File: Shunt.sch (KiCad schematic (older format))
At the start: 1 part

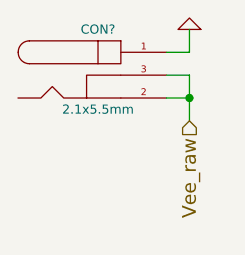
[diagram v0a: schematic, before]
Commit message: breaking out additional subsheets.  specifying transistor values.
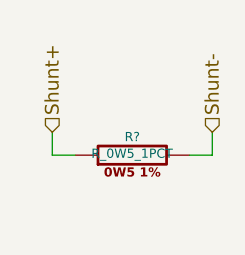
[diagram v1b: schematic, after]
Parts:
- removed CON?: 2.1x5.5mm, ~, symbol BARREL_JACK
- added R?: R_0W5_1PCT, ~, symbol R_0W5_1PCT
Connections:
- new net Shunt+: R?.1
- new net Shunt-: R?.2
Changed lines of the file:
@@
 $Descr A4 11693 8268
 encoding utf-8
-Sheet 5 9
+Sheet 8 9
 Title ""
 Date "29 mar 2014"
@@
 $EndDescr
 $Comp
-L BARREL_JACK CON?
-U 1 1 5337866E
-P 5450 3550
-F 0 "CON?" H 5450 3750 40  0000 C CNN
-F 1 "2.1x5.5mm" H 5450 3400 40  0000 C CNN
-F 2 "~" H 5450 3550 60  0000 C CNN
-F 3 "~" H 5450 3550 60  0000 C CNN
-	1    5450 3550
-	1    0    0    -1
-$EndComp
-$Comp
-L GND #PWR?
-U 1 1 53378674
-P 5850 3350
-F 0 "#PWR?" H 5850 3350 30  0001 C CNN
-F 1 "GND" H 5850 3280 30  0001 C CNN
-F 2 "" H 5850 3350 60  0000 C CNN
-F 3 "" H 5850 3350 60  0000 C CNN
-	1    5850 3350
-	-1   0    0    1
+L R_0W5_1PCT R?
+U 1 1 53383531
+P 5600 3900
+F 0 "R?" V 5680 3900 40  0000 C CNN
+F 1 "R_0W5_1PCT" V 5607 3901 40  0000 C CNN
+F 2 "~" V 5530 3900 30  0000 C CNN
+F 3 "~" H 5600 3900 30  0000 C CNN
+	1    5600 3900
+	0    -1   -1   0
 $EndComp
 Wire Wire Line
-	5750 3450 5850 3450
+	5250 3800 5250 3900
 Wire Wire Line
-	5850 3450 5850 3350
+	5950 3800 5950 3900
 Wire Wire Line
-	5750 3650 5850 3650
+	5250 3900 5350 3900
 Wire Wire Line
-	5850 3550 5850 3750
-Wire Wire Line
-	5750 3550 5850 3550
-Connection ~ 5850 3650
-Text HLabel 5850 3750 3    60   Input ~ 0
-Vee_raw
+	5950 3900 5850 3900
+Text HLabel 5250 3800 1    60   Input ~ 0
+Shunt+
+Text HLabel 5950 3800 1    60   Input ~ 0
+Shunt-
 $EndSCHEMATC

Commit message: working on revamp of power supply.
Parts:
- removed R?: R_0W5_1PCT, ~, symbol R_0W5_1PCT
- added R? (x10): 1, ~, symbol R_0W25_1PCT
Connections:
- net Shunt+: now also R?.1, R?.1, R?.1, R?.1, R?.1, R?.1, R?.1, R?.1, R?.1, R?.1
- net Shunt-: now also R?.2, R?.2, R?.2, R?.2, R?.2, R?.2, R?.2, R?.2, R?.2, R?.2
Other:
- note added: "0.1 Ohm, 2.5 Watt shunt\n(5A max)"
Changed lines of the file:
@@
 EESchema Schematic File Version 2
+LIBS:references_PL
+LIBS:OpAmpPassXsistorBenchSupply-cache
 LIBS:opamps_PL
+LIBS:opto_PL
+LIBS:regulators_PL
+LIBS:relays_PL
+LIBS:resistors_PL
+LIBS:switches_PL
 LIBS:transistors_PL
+LIBS:analog_ICs_PL
+LIBS:capacitors_PL
+LIBS:connectors_PL
 LIBS:diodes_PL
-LIBS:resistors_PL
-LIBS:capacitors_PL
-LIBS:regulators_PL
-LIBS:connectors_PL
+LIBS:displays_PL
+LIBS:LEDs_PL
+LIBS:microcontrollers_PL
+LIBS:mounting_holes_PL
 LIBS:power
 LIBS:device
@@
 $Descr A4 11693 8268
 encoding utf-8
-Sheet 8 9
+Sheet 4 2
 Title ""
 Date "4 jul 2014"
@@
 Comment4 ""
 $EndDescr
-$Comp
-L R_0W5_1PCT R?
-U 1 1 53383531
+Wire Wire Line
+	5150 3800 5150 3900
+Wire Wire Line
+	6050 3800 6050 3900
+Wire Wire Line
+	5150 3900 5350 3900
+Wire Wire Line
+	6050 3900 5850 3900
+Text HLabel 5150 3800 1    60   Input ~ 0
+Shunt+
+Text HLabel 6050 3800 1    60   Input ~ 0
+Shunt-
+$Comp
+L R_0W25_1PCT R?
+U 1 1 53B6360E
 P 5600 3900
 F 0 "R?" V 5680 3900 40  0000 C CNN
-F 1 "R_0W5_1PCT" V 5607 3901 40  0000 C CNN
+F 1 "1" V 5607 3901 40  0000 C CNN
 F 2 "~" V 5530 3900 30  0000 C CNN
 F 3 "~" H 5600 3900 30  0000 C CNN
@@
 	0    -1   -1   0
 $EndComp
-Wire Wire Line
-	5250 3800 5250 3900
-Wire Wire Line
-	5950 3800 5950 3900
-Wire Wire Line
-	5250 3900 5350 3900
-Wire Wire Line
-	5950 3900 5850 3900
-Text HLabel 5250 3800 1    60   Input ~ 0
-Shunt+
-Text HLabel 5950 3800 1    60   Input ~ 0
-Shunt-
+$Comp
+L R_0W25_1PCT R?
+U 1 1 53B63620
+P 5600 4150
+F 0 "R?" V 5680 4150 40  0000 C CNN
+F 1 "1" V 5607 4151 40  0000 C CNN
+F 2 "~" V 5530 4150 30  0000 C CNN
+F 3 "~" H 5600 4150 30  0000 C CNN
+	1    5600 4150
+	0    -1   -1   0
+$EndComp
+$Comp
+L R_0W25_1PCT R?
+U 1 1 53B63626
+P 5600 4400
+F 0 "R?" V 5680 4400 40  0000 C CNN
+F 1 "1" V 5607 4401 40  0000 C CNN
+F 2 "~" V 5530 4400 30  0000 C CNN
+F 3 "~" H 5600 4400 30  0000 C CNN
+	1    5600 4400
+	0    -1   -1   0
+$EndComp
+$Comp
+L R_0W25_1PCT R?
+U 1 1 53B6362C
+P 5600 3650
+F 0 "R?" V 5680 3650 40  0000 C CNN
+F 1 "1" V 5607 3651 40  0000 C CNN
+F 2 "~" V 5530 3650 30  0000 C CNN
+F 3 "~" H 5600 3650 30  0000 C CNN
+	1    5600 3650
+	0    -1   -1   0
+$EndComp
+$Comp
+L R_0W25_1PCT R?
+U 1 1 53B63632
+P 5600 3400
+F 0 "R?" V 5680 3400 40  0000 C CNN
+F 1 "1" V 5607 3401 40  0000 C CNN
+F 2 "~" V 5530 3400 30  0000 C CNN
+F 3 "~" H 5600 3400 30  0000 C CNN
+	1    5600 3400
+	0    -1   -1   0
+$EndComp
+$Comp
+L R_0W25_1PCT R?
+U 1 1 53B63638
+P 5600 4650
+F 0 "R?" V 5680 4650 40  0000 C CNN
+F 1 "1" V 5607 4651 40  0000 C CNN
+F 2 "~" V 5530 4650 30  0000 C CNN
+F 3 "~" H 5600 4650 30  0000 C CNN
+	1    5600 4650
+	0    -1   -1   0
+$EndComp
+$Comp
+L R_0W25_1PCT R?
+U 1 1 53B6363E
+P 5600 4900
+F 0 "R?" V 5680 4900 40  0000 C CNN
+F 1 "1" V 5607 4901 40  0000 C CNN
+F 2 "~" V 5530 4900 30  0000 C CNN
+F 3 "~" H 5600 4900 30  0000 C CNN
+	1    5600 4900
+	0    -1   -1   0
+$EndComp
+$Comp
+L R_0W25_1PCT R?
+U 1 1 53B63644
+P 5600 3150
+F 0 "R?" V 5680 3150 40  0000 C CNN
+F 1 "1" V 5607 3151 40  0000 C CNN
+F 2 "~" V 5530 3150 30  0000 C CNN
+F 3 "~" H 5600 3150 30  0000 C CNN
+	1    5600 3150
+	0    -1   -1   0
+$EndComp
+$Comp
+L R_0W25_1PCT R?
+U 1 1 53B6364A
+P 5600 2900
+F 0 "R?" V 5680 2900 40  0000 C CNN
+F 1 "1" V 5607 2901 40  0000 C CNN
+F 2 "~" V 5530 2900 30  0000 C CNN
+F 3 "~" H 5600 2900 30  0000 C CNN
+	1    5600 2900
+	0    -1   -1   0
+$EndComp
+$Comp
+L R_0W25_1PCT R?
+U 1 1 53B63650
+P 5600 2650
+F 0 "R?" V 5680 2650 40  0000 C CNN
+F 1 "1" V 5607 2651 40  0000 C CNN
+F 2 "~" V 5530 2650 30  0000 C CNN
+F 3 "~" H 5600 2650 30  0000 C CNN
+	1    5600 2650
+	0    -1   -1   0
+$EndComp
+Wire Wire Line
+	5350 2650 5350 2900
+Wire Wire Line
+	5350 2900 5350 3150
+Wire Wire Line
+	5350 3150 5350 3400
+Wire Wire Line
+	5350 3400 5350 3650
+Wire Wire Line
+	5350 3650 5350 3900
+Wire Wire Line
+	5350 3900 5350 4150
+Wire Wire Line
+	5350 4150 5350 4400
+Wire Wire Line
+	5350 4400 5350 4650
+Wire Wire Line
+	5350 4650 5350 4900
+Connection ~ 5350 2900
+Connection ~ 5350 3150
+Connection ~ 5350 3400
+Connection ~ 5350 3650
+Wire Wire Line
+	5850 2650 5850 2900
+Wire Wire Line
+	5850 2900 5850 3150
+Wire Wire Line
+	5850 3150 5850 3400
+Wire Wire Line
+	5850 3400 5850 3650
+Wire Wire Line
+	5850 3650 5850 3900
+Wire Wire Line
+	5850 3900 5850 4150
+Wire Wire Line
+	5850 4150 5850 4400
+Wire Wire Line
+	5850 4400 5850 4650
+Wire Wire Line
+	5850 4650 5850 4900
+Connection ~ 5850 2900
+Connection ~ 5850 3150
+Connection ~ 5850 3400
+Connection ~ 5850 3650
+Connection ~ 5850 3900
+Connection ~ 5350 3900
+Connection ~ 5850 4150
+Connection ~ 5350 4150
+Connection ~ 5850 4400
+Connection ~ 5350 4400
+Connection ~ 5850 4650
+Connection ~ 5350 4650
+Text Notes 5350 2450 0    30   ~ 0
+0.1 Ohm, 2.5 Watt shunt\n(5A max)
 $EndSCHEMATC
